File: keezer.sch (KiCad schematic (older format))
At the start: 15 parts, among them J1 Barrel_Jack, J10 REF, J11 Display, J12 Mode Switch, J13 Tare Switch, J14 Rocker Switch, J2 Relay, J3 Fan, J4 Conn_01x03_Female, J5 Conn_01x03_Female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

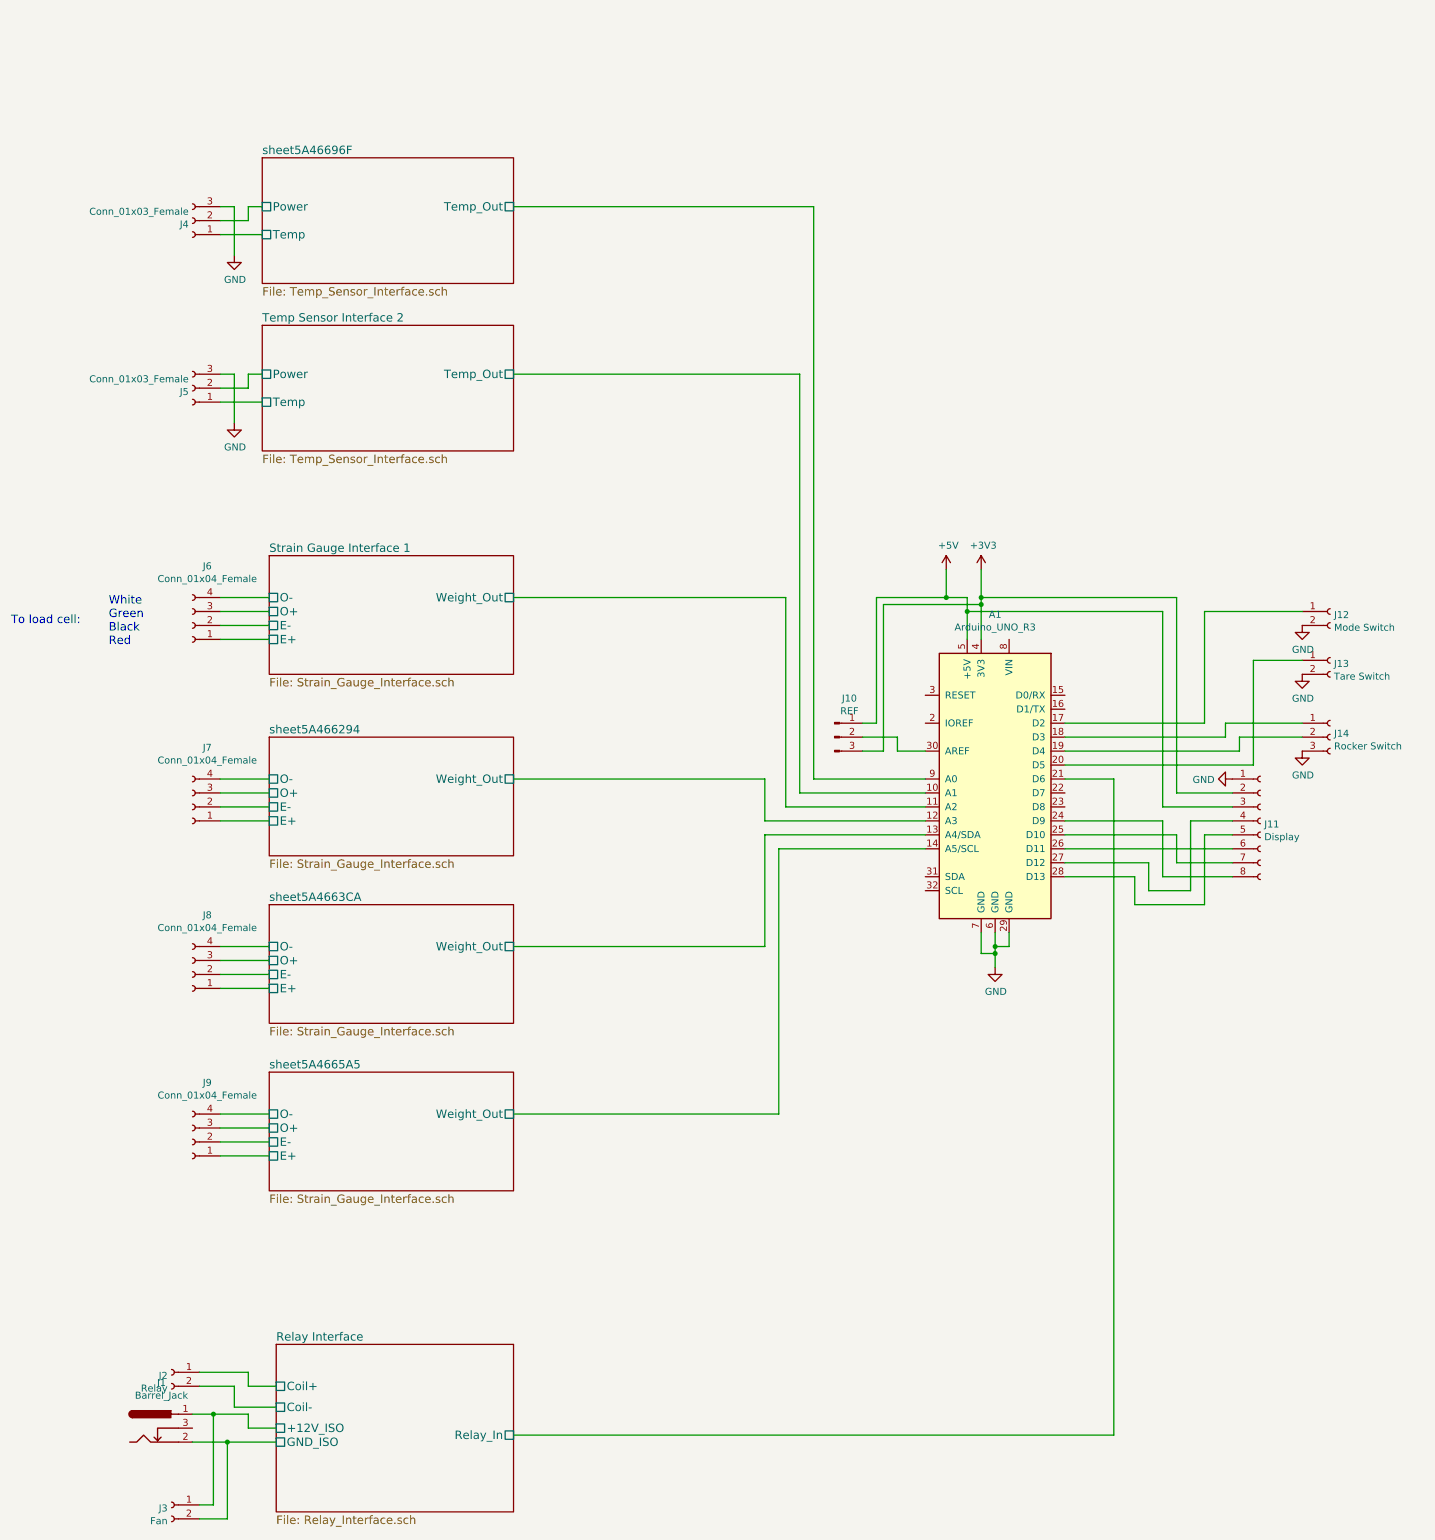
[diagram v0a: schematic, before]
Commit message: Pretty much ready to go. Should verify barrel jack first. Needs a logo.
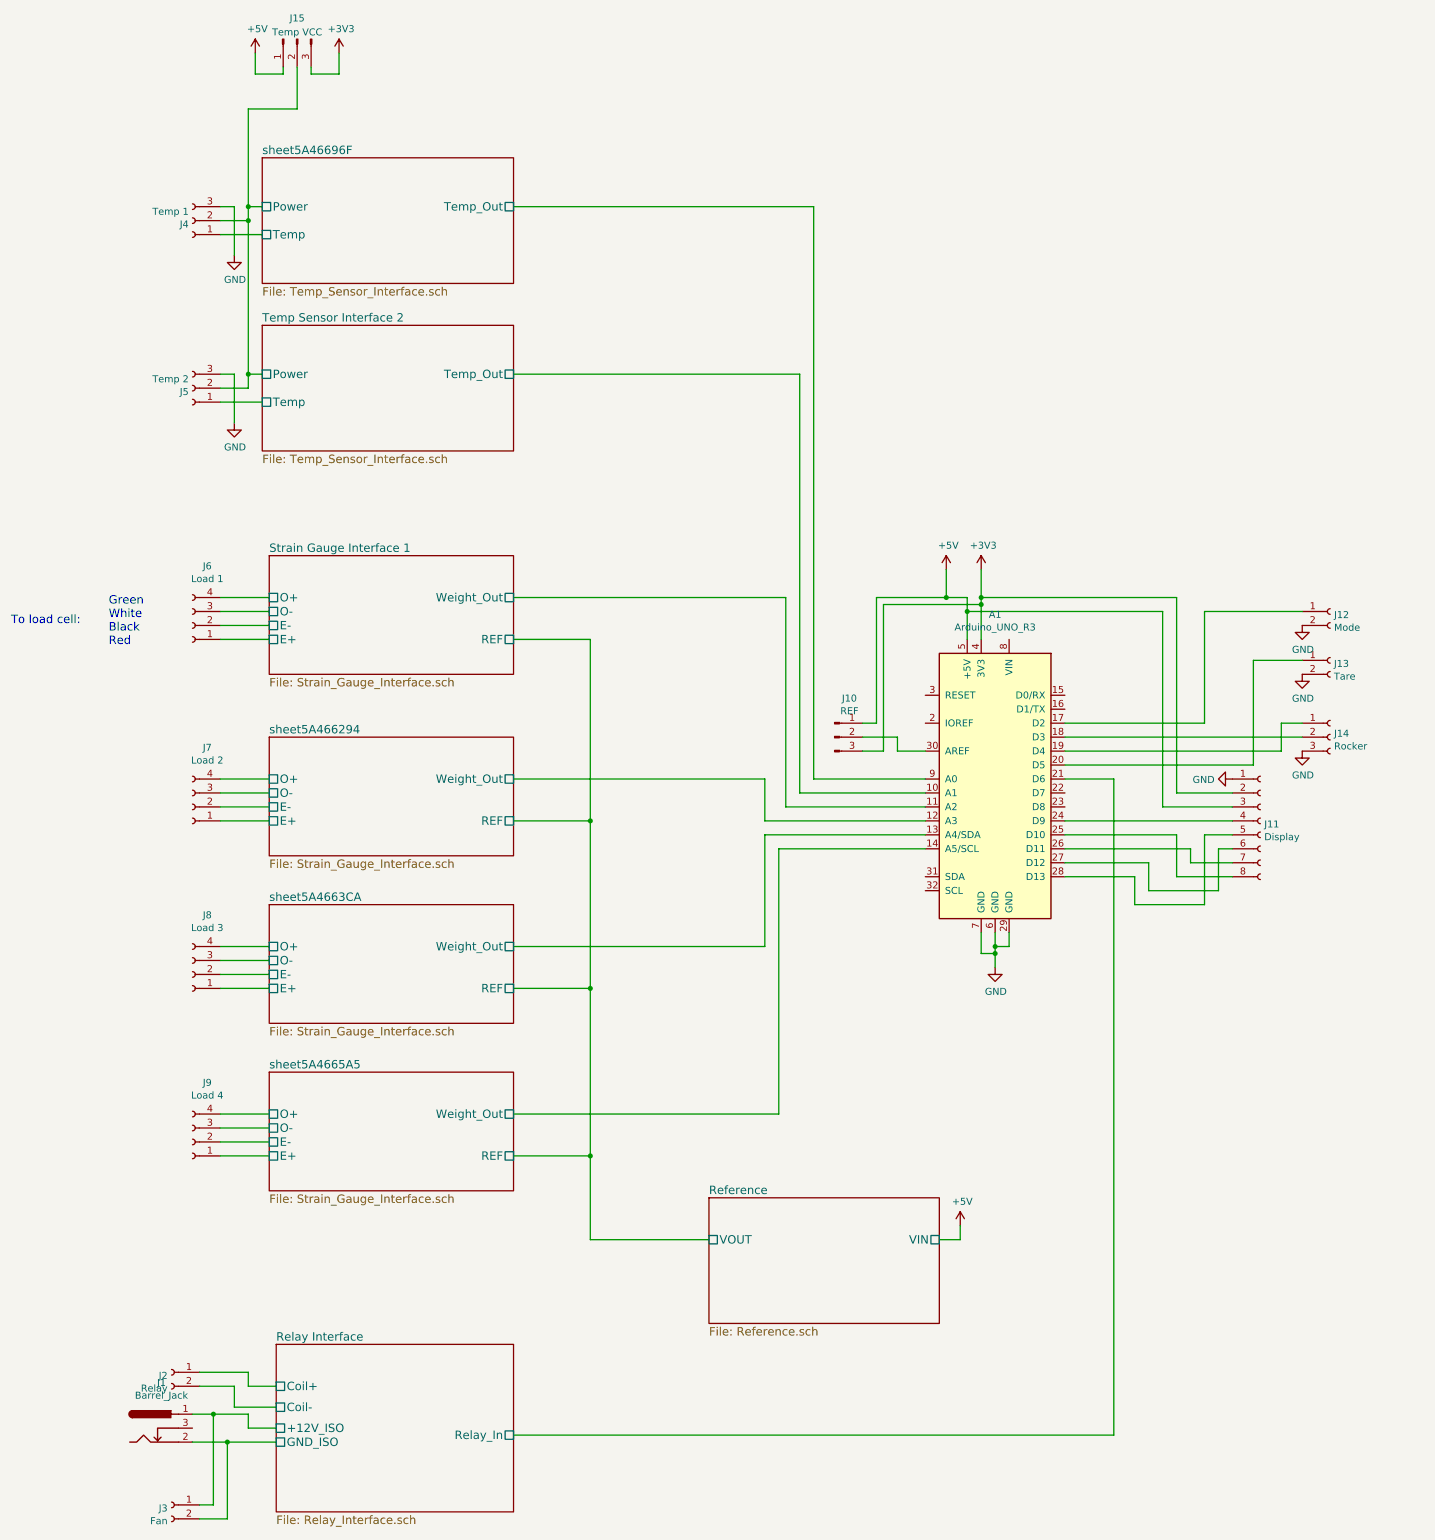
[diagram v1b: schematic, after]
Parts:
- added J15: Temp VCC, Pin_Headers:Pin_Header_Straight_1x03_Pitch2.54mm, symbol Connector:Conn_01x03_Male
- J11: footprint Pin_Headers:Pin_Header_Straight_1x08_Pitch2.54mm -> Connectors_Molex:Molex_NanoFit_2x04x2.50mm_Straight
- J12: value Mode Switch -> Mode; footprint Pin_Headers:Pin_Header_Straight_1x02_Pitch2.54mm -> Connectors_Molex:Molex_NanoFit_1x02x2.50mm_Straight
- J13: value Tare Switch -> Tare; footprint Pin_Headers:Pin_Header_Straight_1x02_Pitch2.54mm -> Connectors_Molex:Molex_NanoFit_1x02x2.50mm_Straight
- J14: value Rocker Switch -> Rocker; footprint Pin_Headers:Pin_Header_Straight_1x03_Pitch2.54mm -> Connectors_Molex:Molex_NanoFit_1x03x2.50mm_Straight
- J2: footprint TerminalBlock_Phoenix:TerminalBlock_Phoenix_MPT-2.54mm_2pol -> Connectors_Molex:Molex_NanoFit_1x02x2.50mm_Straight
- J3: footprint Pin_Headers:Pin_Header_Straight_1x03_Pitch2.54mm -> Connectors_Molex:Molex_NanoFit_1x02x2.50mm_Straight
- J4: value Conn_01x03_Female -> Temp 1; footprint Pin_Headers:Pin_Header_Straight_1x03_Pitch2.54mm -> Connectors_Molex:Molex_NanoFit_1x03x2.50mm_Straight
- J5: value Conn_01x03_Female -> Temp 2; footprint Pin_Headers:Pin_Header_Straight_1x03_Pitch2.54mm -> Connectors_Molex:Molex_NanoFit_1x03x2.50mm_Straight
- J6: value Conn_01x04_Female -> Load 1; footprint Pin_Headers:Pin_Header_Straight_1x04_Pitch2.54mm -> Connectors_Molex:Molex_NanoFit_2x02x2.50mm_Straight
- J7: value Conn_01x04_Female -> Load 2; footprint Pin_Headers:Pin_Header_Straight_1x04_Pitch2.54mm -> Connectors_Molex:Molex_NanoFit_2x02x2.50mm_Straight
- J8: value Conn_01x04_Female -> Load 3; footprint Pin_Headers:Pin_Header_Straight_1x04_Pitch2.54mm -> Connectors_Molex:Molex_NanoFit_2x02x2.50mm_Straight
- J9: value Conn_01x04_Female -> Load 4; footprint Pin_Headers:Pin_Header_Straight_1x04_Pitch2.54mm -> Connectors_Molex:Molex_NanoFit_2x02x2.50mm_Straight
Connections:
- net sheet5A46696F/Power is gone; now on net Temp Sensor Interface 2/Power: J4.2 (Pin_2)
- net +3V3: now also J15.3 (Pin_3)
- net +5V: now also J15.1 (Pin_1)
- net Strain Gauge Interface 1/O+: now also J6.4 (Pin_4); no longer J6.3 (Pin_3)
- net Strain Gauge Interface 1/O-: now also J6.3 (Pin_3); no longer J6.4 (Pin_4)
- net Temp Sensor Interface 2/Power: now also J15.2 (Pin_2)
- net sheet5A466294/O+: now also J7.4 (Pin_4); no longer J7.3 (Pin_3)
- net sheet5A466294/O-: now also J7.3 (Pin_3); no longer J7.4 (Pin_4)
- net sheet5A4663CA/O+: now also J8.4 (Pin_4); no longer J8.3 (Pin_3)
- net sheet5A4663CA/O-: now also J8.3 (Pin_3); no longer J8.4 (Pin_4)
- net sheet5A4665A5/O+: now also J9.4 (Pin_4); no longer J9.3 (Pin_3)
- net sheet5A4665A5/O-: now also J9.3 (Pin_3); no longer J9.4 (Pin_4)
- net at A1.20 (D5), J13.1 (Pin_1): no longer A1.18 (D3), J14.1 (Pin_1)
- net at J14.2 (Pin_2): now also A1.18 (D3); no longer A1.19 (D4)
- net at A1.24 (D9): now also J11.4 (Pin_4); no longer J11.8 (Pin_8)
- net at A1.25 (D10): now also J11.8 (Pin_8); no longer J11.7 (Pin_7)
- net at A1.26 (D11): now also J11.7 (Pin_7); no longer J11.6 (Pin_6)
- net at A1.27 (D12): now also J11.6 (Pin_6); no longer J11.4 (Pin_4)
- new net: A1.19 (D4), J14.1 (Pin_1)
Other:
- note added: "Green\nWhite\nBlack\nRed"
- note removed: "White\nGreen\nBlack\nRed"
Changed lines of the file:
@@
 $Descr A2 23386 16535
 encoding utf-8
-Sheet 1 8
+Sheet 1 9
 Title ""
 Date ""
@@
 F2 "E+" U L 7750 7150 60
 F3 "E-" U L 7750 7050 60
-F4 "O+" U L 7750 6950 60
-F5 "O-" U L 7750 6850 60
+F4 "O+" U L 7750 6850 60
+F5 "O-" U L 7750 6950 60
 F6 "Weight_Out" U R 9500 6850 60
+F7 "REF" U R 9500 7150 60
 $EndSheet
 $Comp
@@
 P 7200 4150
 F 0 "J4" H 7227 4176 50  0000 L CNN
-F 1 "Conn_01x03_Female" H 7227 4085 50  0000 L CNN
-F 2 "Pin_Headers:Pin_Header_Straight_1x03_Pitch2.54mm" H 7200 4150 50  0001 C CNN
+F 1 "Temp 1" H 7227 4085 50  0000 L CNN
+F 2 "Connectors_Molex:Molex_NanoFit_1x03x2.50mm_Straight" H 7200 4150 50  0001 C CNN
 F 3 "~" H 7200 4150 50  0001 C CNN
 	1    7200 4150
@@
 P 7200 5350
 F 0 "J5" H 7227 5376 50  0000 L CNN
-F 1 "Conn_01x03_Female" H 7227 5285 50  0000 L CNN
-F 2 "Pin_Headers:Pin_Header_Straight_1x03_Pitch2.54mm" H 7200 5350 50  0001 C CNN
+F 1 "Temp 2" H 7227 5285 50  0000 L CNN
+F 2 "Connectors_Molex:Molex_NanoFit_1x03x2.50mm_Straight" H 7200 5350 50  0001 C CNN
 F 3 "~" H 7200 5350 50  0001 C CNN
 	1    7200 5350
@@
 P 7200 7050
 F 0 "J6" H 7094 6625 50  0000 C CNN
-F 1 "Conn_01x04_Female" H 7094 6716 50  0000 C CNN
-F 2 "Pin_Headers:Pin_Header_Straight_1x04_Pitch2.54mm" H 7200 7050 50  0001 C CNN
+F 1 "Load 1" H 7094 6716 50  0000 C CNN
+F 2 "Connectors_Molex:Molex_NanoFit_2x02x2.50mm_Straight" H 7200 7050 50  0001 C CNN
 F 3 "~" H 7200 7050 50  0001 C CNN
 	1    7200 7050
@@
 P 7200 8350
 F 0 "J7" H 7094 7925 50  0000 C CNN
-F 1 "Conn_01x04_Female" H 7094 8016 50  0000 C CNN
-F 2 "Pin_Headers:Pin_Header_Straight_1x04_Pitch2.54mm" H 7200 8350 50  0001 C CNN
+F 1 "Load 2" H 7094 8016 50  0000 C CNN
+F 2 "Connectors_Molex:Molex_NanoFit_2x02x2.50mm_Straight" H 7200 8350 50  0001 C CNN
 F 3 "~" H 7200 8350 50  0001 C CNN
 	1    7200 8350
@@
 P 7200 9550
 F 0 "J8" H 7094 9125 50  0000 C CNN
-F 1 "Conn_01x04_Female" H 7094 9216 50  0000 C CNN
-F 2 "Pin_Headers:Pin_Header_Straight_1x04_Pitch2.54mm" H 7200 9550 50  0001 C CNN
+F 1 "Load 3" H 7094 9216 50  0000 C CNN
+F 2 "Connectors_Molex:Molex_NanoFit_2x02x2.50mm_Straight" H 7200 9550 50  0001 C CNN
 F 3 "~" H 7200 9550 50  0001 C CNN
 	1    7200 9550
@@
 P 7200 10750
 F 0 "J9" H 7094 10325 50  0000 C CNN
-F 1 "Conn_01x04_Female" H 7094 10416 50  0000 C CNN
-F 2 "Pin_Headers:Pin_Header_Straight_1x04_Pitch2.54mm" H 7200 10750 50  0001 C CNN
+F 1 "Load 4" H 7094 10416 50  0000 C CNN
+F 2 "Connectors_Molex:Molex_NanoFit_2x02x2.50mm_Straight" H 7200 10750 50  0001 C CNN
 F 3 "~" H 7200 10750 50  0001 C CNN
 	1    7200 10750
@@
 F 0 "J2" H 7078 12376 50  0000 L CNN
 F 1 "Relay" H 7078 12285 50  0000 L CNN
-F 2 "TerminalBlock_Phoenix:TerminalBlock_Phoenix_MPT-2.54mm_2pol" H 7050 12400 50  0001 C CNN
+F 2 "Connectors_Molex:Molex_NanoFit_1x02x2.50mm_Straight" H 7050 12400 50  0001 C CNN
 F 3 "~" H 7050 12400 50  0001 C CNN
 	1    7050 12400
@@
 F2 "E+" U L 7750 8450 60
 F3 "E-" U L 7750 8350 60
-F4 "O+" U L 7750 8250 60
-F5 "O-" U L 7750 8150 60
+F4 "O+" U L 7750 8150 60
+F5 "O-" U L 7750 8250 60
 F6 "Weight_Out" U R 9500 8150 60
+F7 "REF" U R 9500 8450 60
 $EndSheet
 $Sheet
@@
 F2 "E+" U L 7750 9650 60
 F3 "E-" U L 7750 9550 60
-F4 "O+" U L 7750 9450 60
-F5 "O-" U L 7750 9350 60
+F4 "O+" U L 7750 9350 60
+F5 "O-" U L 7750 9450 60
 F6 "Weight_Out" U R 9500 9350 60
+F7 "REF" U R 9500 9650 60
 $EndSheet
 $Sheet
@@
 F2 "E+" U L 7750 10850 60
 F3 "E-" U L 7750 10750 60
-F4 "O+" U L 7750 10650 60
-F5 "O-" U L 7750 10550 60
+F4 "O+" U L 7750 10550 60
+F5 "O-" U L 7750 10650 60
 F6 "Weight_Out" U R 9500 10550 60
+F7 "REF" U R 9500 10850 60
 $EndSheet
 $Sheet
@@
 F 0 "J11" H 14878 8426 50  0000 L CNN
 F 1 "Display" H 14878 8335 50  0000 L CNN
-F 2 "Pin_Headers:Pin_Header_Straight_1x08_Pitch2.54mm" H 14850 8450 50  0001 C CNN
+F 2 "Connectors_Molex:Molex_NanoFit_2x04x2.50mm_Straight" H 14850 8450 50  0001 C CNN
 F 3 "~" H 14850 8450 50  0001 C CNN
 	1    14850 8450
@@
 P 15350 6950
 F 0 "J12" H 15378 6926 50  0000 L CNN
-F 1 "Mode Switch" H 15378 6835 50  0000 L CNN
-F 2 "Pin_Headers:Pin_Header_Straight_1x02_Pitch2.54mm" H 15350 6950 50  0001 C CNN
+F 1 "Mode" H 15378 6835 50  0000 L CNN
+F 2 "Connectors_Molex:Molex_NanoFit_1x02x2.50mm_Straight" H 15350 6950 50  0001 C CNN
 F 3 "~" H 15350 6950 50  0001 C CNN
 	1    15350 6950
@@
 P 15350 7300
 F 0 "J13" H 15377 7276 50  0000 L CNN
-F 1 "Tare Switch" H 15377 7185 50  0000 L CNN
-F 2 "Pin_Headers:Pin_Header_Straight_1x02_Pitch2.54mm" H 15350 7300 50  0001 C CNN
+F 1 "Tare" H 15377 7185 50  0000 L CNN
+F 2 "Connectors_Molex:Molex_NanoFit_1x02x2.50mm_Straight" H 15350 7300 50  0001 C CNN
 F 3 "~" H 15350 7300 50  0001 C CNN
 	1    15350 7300
@@
 P 15350 7850
 F 0 "J14" H 15378 7876 50  0000 L CNN
-F 1 "Rocker Switch" H 15378 7785 50  0000 L CNN
-F 2 "Pin_Headers:Pin_Header_Straight_1x03_Pitch2.54mm" H 15350 7850 50  0001 C CNN
+F 1 "Rocker" H 15378 7785 50  0000 L CNN
+F 2 "Connectors_Molex:Molex_NanoFit_1x03x2.50mm_Straight" H 15350 7850 50  0001 C CNN
 F 3 "~" H 15350 7850 50  0001 C CNN
 	1    15350 7850
@@
 F 0 "J3" H 7078 13326 50  0000 L CNN
 F 1 "Fan" H 7078 13235 50  0000 L CNN
-F 2 "Pin_Headers:Pin_Header_Straight_1x03_Pitch2.54mm" H 7050 13350 50  0001 C CNN
+F 2 "Connectors_Molex:Molex_NanoFit_1x02x2.50mm_Straight" H 7050 13350 50  0001 C CNN
 F 3 "~" H 7050 13350 50  0001 C CNN
 	1    7050 13350
@@
 	14650 8350 14150 8350
 Wire Wire Line
-	14650 8850 14150 8850
-Wire Wire Line
-	14150 8850 14150 8450
-Wire Wire Line
-	13450 8450 14150 8450
-Wire Wire Line
-	14250 8550 14250 8750
-Wire Wire Line
-	14250 8750 14650 8750
-Wire Wire Line
 	13450 8550 14250 8550
 Wire Wire Line
-	13450 8650 14650 8650
-Wire Wire Line
 	14050 8750 14050 8950
-Wire Wire Line
-	14050 8950 14350 8950
-Wire Wire Line
-	14350 8950 14350 8450
-Wire Wire Line
-	14350 8450 14650 8450
 Wire Wire Line
 	13450 8750 14050 8750
@@
 	14450 7750 13450 7750
 Wire Wire Line
-	13450 7850 14600 7850
-Wire Wire Line
-	14600 7850 14600 7750
-Wire Wire Line
-	14600 7750 14800 7750
-Wire Wire Line
-	15150 7850 14700 7850
-Wire Wire Line
-	14700 7850 14700 7950
-Wire Wire Line
-	14700 7950 13450 7950
-Wire Wire Line
-	13450 8050 14800 8050
-Wire Wire Line
-	14800 7750 15150 7750
-Wire Wire Line
-	14800 8050 14800 7750
-Wire Wire Line
 	14800 7300 15150 7300
-Wire Wire Line
-	14800 7750 14800 7300
 Wire Wire Line
 	13800 8150 13450 8150
@@
 	7400 8450 7750 8450
 Text Notes 6600 7200 0    60   ~ 0
-White\nGreen\nBlack\nRed
+Green\nWhite\nBlack\nRed
 Text Notes 5900 7050 0    60   ~ 0
 To load cell:
@@
 Wire Wire Line
 	7500 5250 7500 5600
+$Sheet
+S 10900 11150 1650 900
+U 5A486C54
+F0 "Reference" 60
+F1 "Reference.sch" 60
+F2 "VIN" U R 12550 11450 60
+F3 "VOUT" U L 10900 11450 60
+$EndSheet
+$Comp
+L power:+5V #PWR037
+U 1 1 5A48F52C
+P 12700 11350
+F 0 "#PWR037" H 12700 11200 50  0001 C CNN
+F 1 "+5V" H 12715 11523 50  0000 C CNN
+F 2 "" H 12700 11350 50  0001 C CNN
+F 3 "" H 12700 11350 50  0001 C CNN
+	1    12700 11350
+	1    0    0    -1
+$EndComp
+Wire Wire Line
+	12550 11450 12700 11450
+Wire Wire Line
+	12700 11450 12700 11350
+Wire Wire Line
+	10900 11450 10050 11450
+Wire Wire Line
+	10050 11450 10050 10850
+Wire Wire Line
+	10050 10850 9500 10850
+Wire Wire Line
+	10050 10850 10050 9650
+Wire Wire Line
+	10050 9650 9500 9650
+Connection ~ 10050 10850
+Wire Wire Line
+	10050 9650 10050 8450
+Wire Wire Line
+	10050 8450 9500 8450
+Connection ~ 10050 9650
+Wire Wire Line
+	10050 8450 10050 7150
+Wire Wire Line
+	10050 7150 9500 7150
+Connection ~ 10050 8450
+$Comp
+L Connector:Conn_01x03_Male J15
+U 1 1 5A49466C
+P 7950 2850
+F 0 "J15" V 7800 2850 50  0000 C CNN
+F 1 "Temp VCC" V 7900 2850 50  0000 C CNN
+F 2 "Pin_Headers:Pin_Header_Straight_1x03_Pitch2.54mm" H 7950 2850 50  0001 C CNN
+F 3 "~" H 7950 2850 50  0001 C CNN
+	1    7950 2850
+	0    -1   1    0
+$EndComp
+$Comp
+L power:+3V3 #PWR09
+U 1 1 5A4B2627
+P 8250 2950
+F 0 "#PWR09" H 8250 2800 50  0001 C CNN
+F 1 "+3V3" H 8265 3123 50  0000 C CNN
+F 2 "" H 8250 2950 50  0001 C CNN
+F 3 "" H 8250 2950 50  0001 C CNN
+	1    8250 2950
+	1    0    0    -1
+$EndComp
+$Comp
+L power:+5V #PWR010
+U 1 1 5A4B2B7E
+P 7650 2950
+F 0 "#PWR010" H 7650 2800 50  0001 C CNN
+F 1 "+5V" H 7665 3123 50  0000 C CNN
+F 2 "" H 7650 2950 50  0001 C CNN
+F 3 "" H 7650 2950 50  0001 C CNN
+	1    7650 2950
+	1    0    0    -1
+$EndComp
+Wire Wire Line
+	8050 3100 8050 3050
+Wire Wire Line
+	7650 3100 7850 3100
+Wire Wire Line
+	7850 3100 7850 3050
+Wire Wire Line
+	7650 2950 7650 3100
+Wire Wire Line
+	7600 4050 7600 3350
+Wire Wire Line
+	7600 3350 7950 3350
+Wire Wire Line
+	7950 3350 7950 3050
+Connection ~ 7600 4050
+Wire Wire Line
+	7600 4150 7600 5250
+Connection ~ 7600 4150
+Connection ~ 7600 5250
+Wire Wire Line
+	8250 3100 8250 2950
+Wire Wire Line
+	8050 3100 8250 3100
+Wire Wire Line
+	13450 8450 14650 8450
+Wire Wire Line
+	14250 8850 14650 8850
+Wire Wire Line
+	14250 8550 14250 8850
+Wire Wire Line
+	13450 8650 14350 8650
+Wire Wire Line
+	14350 8650 14350 8750
+Wire Wire Line
+	14350 8750 14650 8750
+Wire Wire Line
+	14550 8950 14550 8650
+Wire Wire Line
+	14550 8650 14650 8650
+Wire Wire Line
+	14050 8950 14550 8950
+Wire Wire Line
+	13450 8050 14800 8050
+Wire Wire Line
+	14800 7300 14800 8050
+Wire Wire Line
+	15000 7950 15000 7750
+Wire Wire Line
+	15000 7750 15150 7750
+Wire Wire Line
+	13450 7950 15000 7950
+Wire Wire Line
+	13450 7850 15150 7850
 $EndSCHEMATC
